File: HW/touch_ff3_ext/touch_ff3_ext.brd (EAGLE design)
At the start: 42.5 x 28.4 mm, 18 parts, among them J3 AVR_SPI_PRG_6PTH, M1 SMALL_SERVO, Q2 MOSFET-PCHANNEL, U1 MCP73831, X1 USBSMD

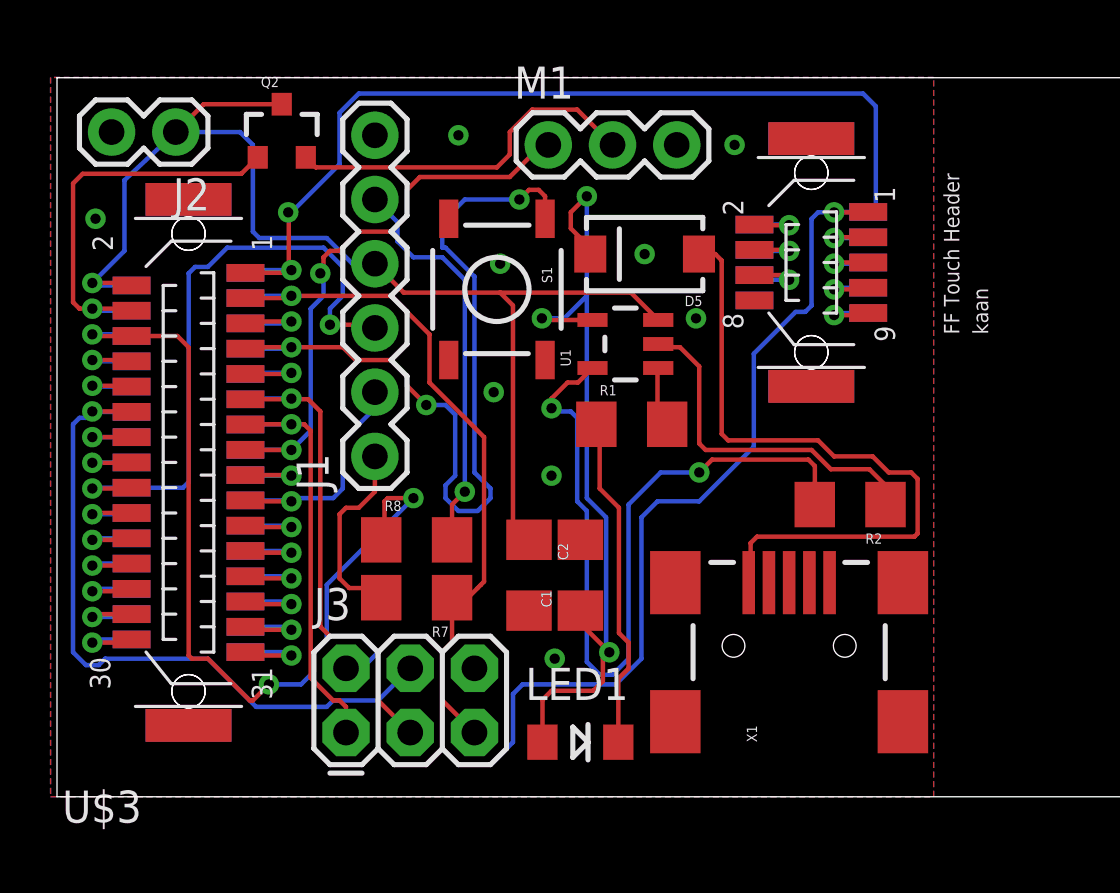
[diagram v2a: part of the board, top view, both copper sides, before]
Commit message: change vdd/vunreg wire widths
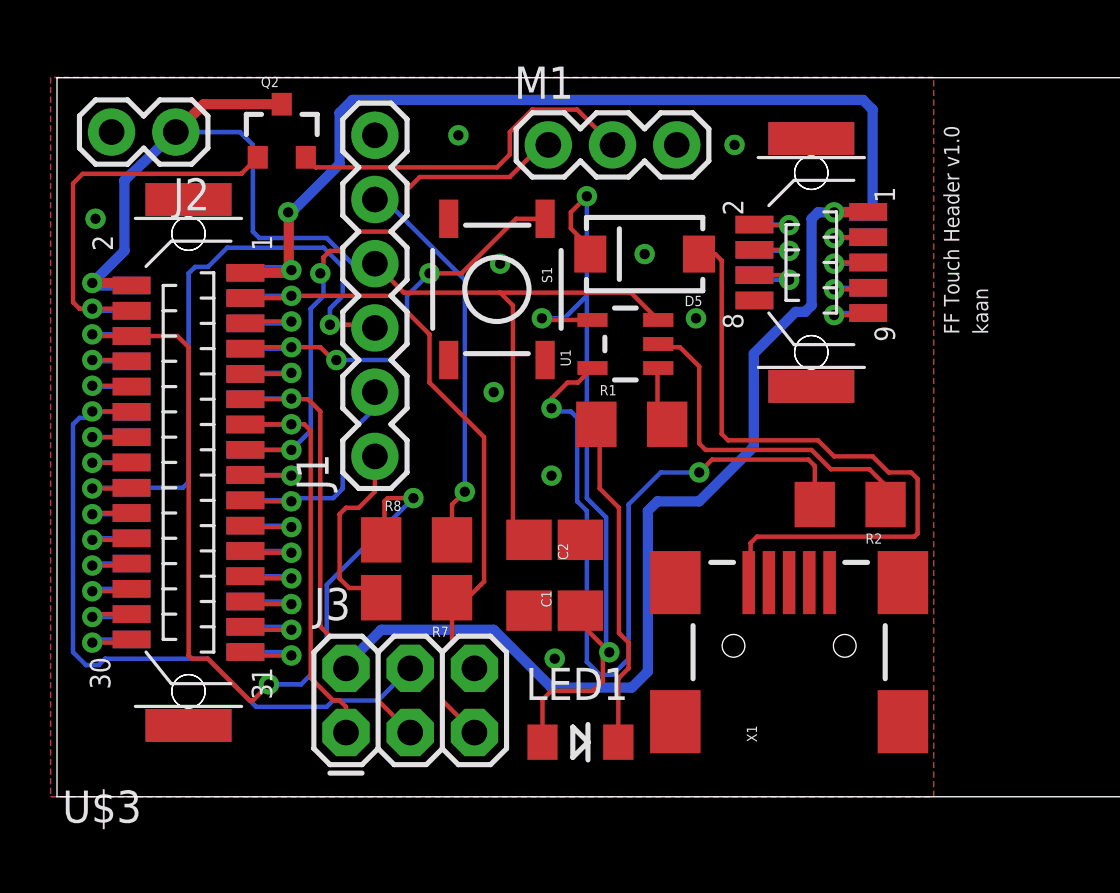
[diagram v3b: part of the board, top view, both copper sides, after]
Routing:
- net PD1: track 34.7 -> 17.5 mm
- net VDD: track 81.5 -> 75.9 mm
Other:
- board text added: "FF Touch Header v1.0"
- board text removed: "FF Touch Header"

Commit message: updated pcb, added servo on off code
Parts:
- removed J1: (no value), SparkFun-Connectors:1X06
- removed Q2: MOSFET-PCHANNEL, SparkFun-DiscreteSemi:SOT23-3
- removed R7, R8: 0, SparkFun-Passives:1206
- removed S1: SWITCH-MOMENTARY-2SMD, SparkFun-Electromechanical:TACTILE-SWITCH-SMD
- added Q1: MOSFET-NCHANNELBSS123LT1G, SparkFun-DiscreteSemi:SOT23-3
- added R3: 100, SparkFun-Passives:1206
- added R4: 1k, SparkFun-Passives:1206
- added S2: (no value), SparkFun-Electromechanical:SWITCH-SPST-SMD-A
- moved C2 0.25 mm to (42.9, 26.3)
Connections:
- removed net N$1: R2.1, U1.2
- removed net N$18: J1.1, R7.2
- removed net N$19: J1.5, R8.2
- new net N$3: Q1.1, R3.2, R4.2
- new net V_BAT: C2.1, J2.1, S2.2, U1.3
- net GND: now also Q1.2, R2.1, R4.1, U1.2; no longer J1.6, M1.3, S1.3
- net N$2: now also M1.3, Q1.3; no longer M1.2, Q2.2
- net PD1: no longer S1.1
- net PG0: now also R3.1; no longer Q2.1
- net RST: no longer R7.1
- net RX0_MCU: no longer J1.3
- net SCL: no longer R8.1
- net TX0_MCU: no longer J1.2
- net V_UNREG: now also M1.2, S2.3; no longer C2.1, J1.4, J2.1, Q2.3, U1.3
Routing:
- net V_BAT: track 0.00 -> 35.4 mm
- net SCL: track 35.7 -> 3.25 mm, vias 3 -> 1
- net RX0_MCU: track 24.9 -> 3.13 mm, vias 2 -> 1
- net VDD: track 75.9 -> 59.2 mm
- net V_UNREG: track 49.6 -> 33.1 mm, vias 1 -> 2
- net N$19: track 15.4 -> 0.00 mm, vias 1 -> 0
- net N$1: track 14.0 -> 0.00 mm
- net GND: track 3.75 -> 17.8 mm, vias 10 -> 7
- net PD1: track 17.5 -> 3.69 mm, vias 3 -> 1
- net N$3: track 0.00 -> 8.45 mm
- net N$18: track 7.67 -> 0.00 mm
- net TX0_MCU: track 10.3 -> 3.90 mm
- net PG0: track 16.5 -> 21.1 mm
- net N$6: track 33.3 -> 30.4 mm
- net RST: track 28.0 -> 26.0 mm
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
